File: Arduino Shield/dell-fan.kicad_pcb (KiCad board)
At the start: 2 copper layers, 101.6 x 53.3 mm, 50 parts, among them J1 Power, P1 Digital, P10 CONN_01X01, P11 CONN_01X01, P13 CONN_01X01, P2 Power, P3 Analog, P4 Analog, P5 PWM, P6 PWM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

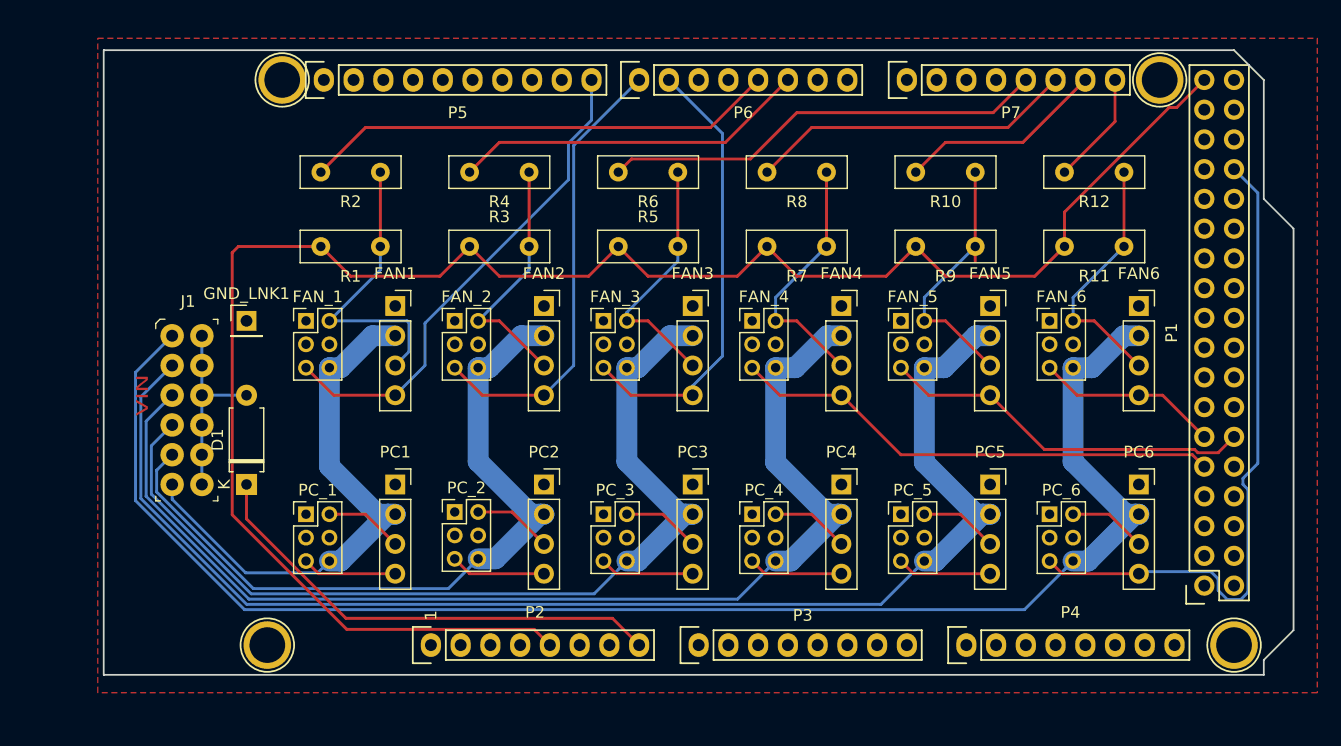
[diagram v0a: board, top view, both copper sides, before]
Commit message: moved PC Tach and PWM to D554-d69
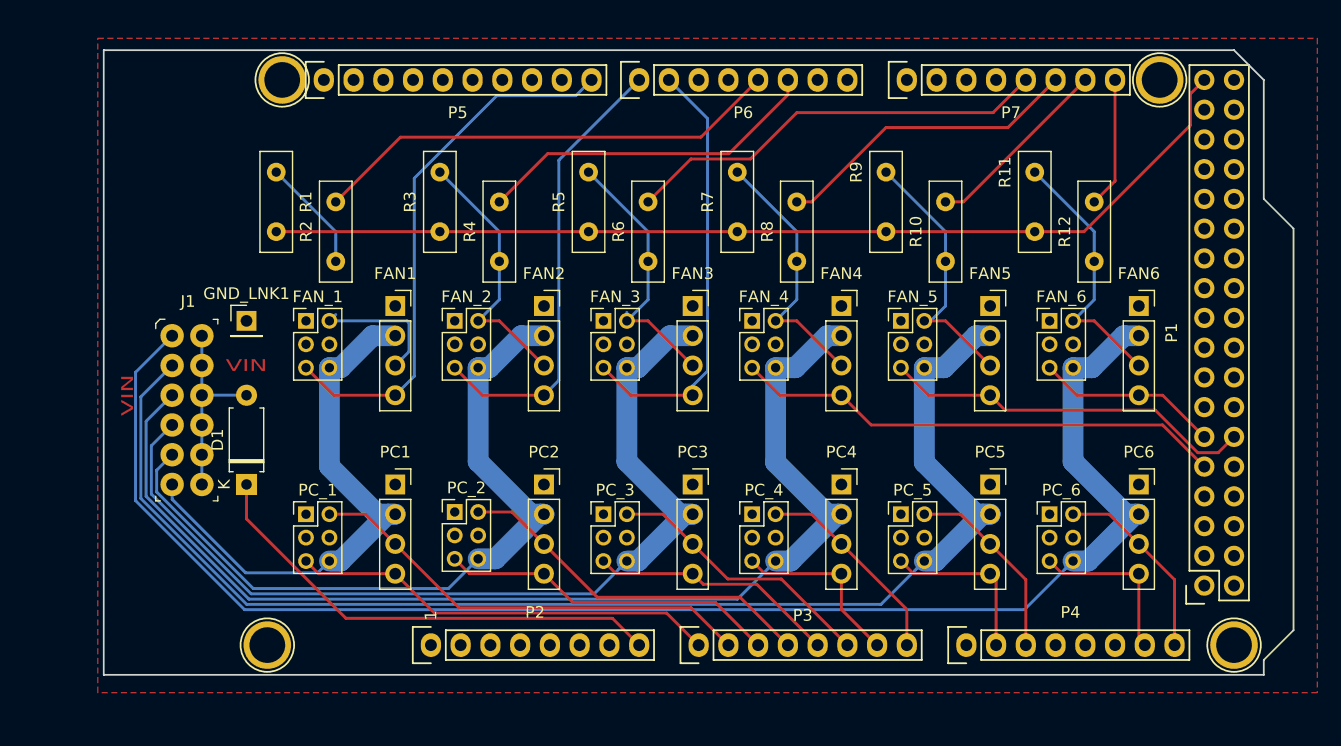
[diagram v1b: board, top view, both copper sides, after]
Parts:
- moved R1 10.9 mm to (118.1, 78.7), turned to 270 degrees
- moved R11 9.92 mm to (182.9, 78.7), turned to 270 degrees
- moved R5 9.92 mm to (144.8, 78.7), turned to 270 degrees
- moved R7 9.92 mm to (157.5, 78.7), turned to 270 degrees
- moved R9 9.92 mm to (170.2, 78.7), turned to 270 degrees
- moved R3 9.92 mm to (132.1, 78.7), turned to 270 degrees
- moved R2 8.52 mm to (123.2, 86.4), turned to 90 degrees
- moved R10 8.03 mm to (175.3, 86.4), turned to 90 degrees
- moved R12 8.03 mm to (188.0, 86.4), turned to 90 degrees
- moved R4 8.03 mm to (137.2, 86.4), turned to 90 degrees
- moved R6 8.03 mm to (149.9, 86.4), turned to 90 degrees
- moved R8 8.03 mm to (162.6, 86.4), turned to 90 degrees
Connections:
- P1 pad 19: PC5_TACH -> (no net)
- P1 pad 20: PC6_TACH -> (no net)
- P1 pad 21: PC3_TACH -> (no net)
- P1 pad 22: PC4_TACH -> (no net)
- P1 pad 23: PC1_TACH -> (no net)
- P1 pad 24: PC2_TACH -> (no net)
- P1 pad 29: PC5_PWM -> (no net)
- P1 pad 30: PC6_PWM -> (no net)
- P1 pad 31: PC3_PWM -> (no net)
- P1 pad 32: PC4_PWM -> (no net)
- P1 pad 33: PC1_PWM -> (no net)
- P1 pad 34: PC2_PWM -> (no net)
- P3 pad 1: (no net) -> PC1_PWM
- P3 pad 2: (no net) -> PC1_TACH
- P3 pad 3: (no net) -> PC2_PWM
- P3 pad 4: (no net) -> PC2_TACH
- P3 pad 5: (no net) -> PC3_PWM
- P3 pad 6: (no net) -> PC3_TACH
- P3 pad 7: (no net) -> PC4_PWM
- P3 pad 8: (no net) -> PC4_TACH
- P4 pad 2: (no net) -> PC5_PWM
- P4 pad 3: (no net) -> PC5_TACH
- P4 pad 7: (no net) -> PC6_PWM
- P4 pad 8: (no net) -> PC6_TACH
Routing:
- net +5V: track 155.5 -> 86.2 mm
- net PC6_PWM: track 56.9 -> 14.4 mm
- net PC1_TACH: track 6.67 -> 38.7 mm
- net PC1_PWM: track 8.07 -> 36.5 mm
- net PC2_TACH: track 6.75 -> 31.2 mm
- net PC2_PWM: track 8.15 -> 29.0 mm
- net PC3_TACH: track 6.67 -> 23.5 mm
- net PC3_PWM: track 8.07 -> 21.3 mm
- net PC4_TACH: track 6.67 -> 17.6 mm
- net PC6_TACH: track 6.67 -> 16.6 mm
- net PC5_TACH: track 6.67 -> 16.6 mm
- net PC4_PWM: track 8.07 -> 15.4 mm
- net PC5_PWM: track 8.07 -> 14.4 mm
- net FAN1_TACH_IN: track 25.5 -> 21.5 mm
- net FAN1_PWM: track 42.5 -> 46.4 mm
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
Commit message: fixed ground plane issue
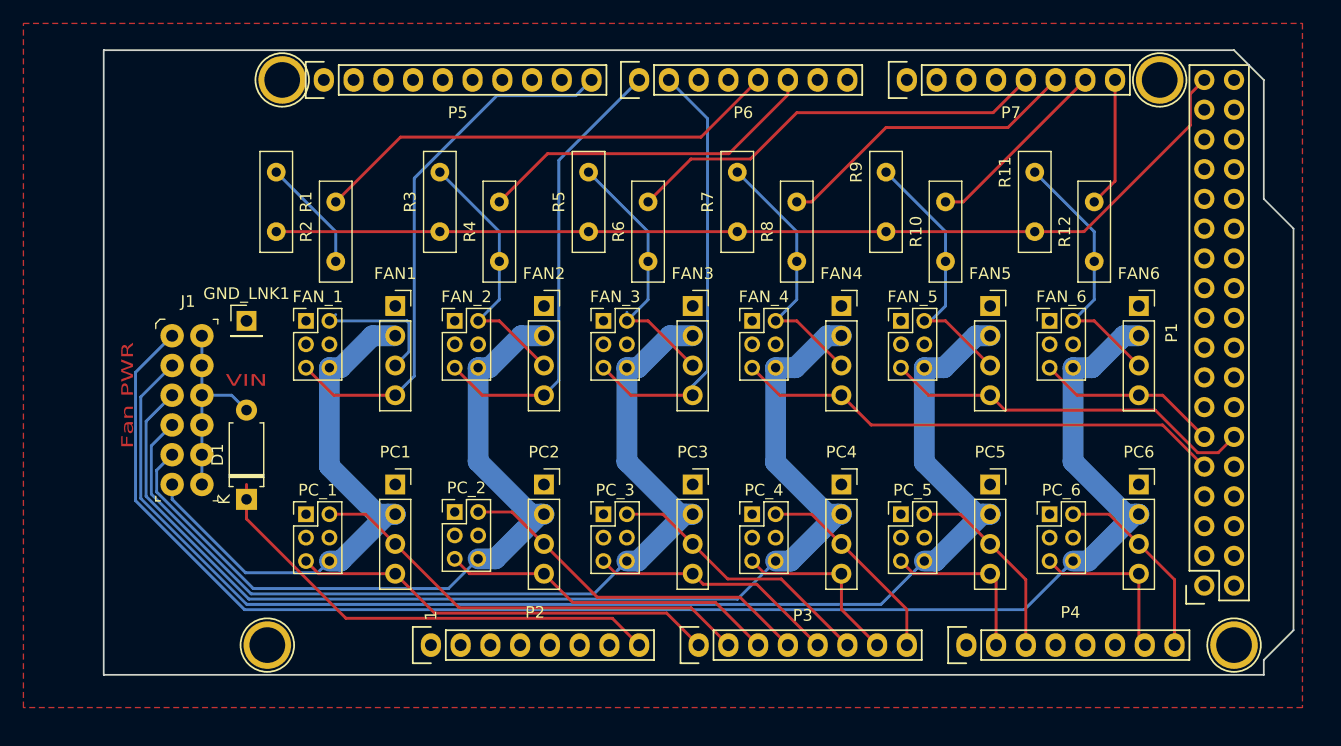
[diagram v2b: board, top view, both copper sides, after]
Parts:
- moved D1 1.27 mm to (115.6, 106.7)
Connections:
- P2 pad 5: +5V -> (no net)
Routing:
- net Net-(D1-Pad2): track 16.5 -> 17.0 mm
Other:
- board text added: "Fan PWR"
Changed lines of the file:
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@@
     (thickness 1.6)
     (drawings 20)
-    (tracks 249)
+    (tracks 250)
     (zones 0)
     (modules 50)
@@
     (add_net "Net-(P13-Pad1)")
     (add_net "Net-(P2-Pad1)")
+    (add_net "Net-(P2-Pad5)")
     (add_net "Net-(P8-Pad1)")
     (add_net "Net-(PC_1-Pad3)")
@@
   )
   (module Diode_THT:D_A-405_P7.62mm_Horizontal placed (layer F.Cu)
-    (at 115.57 105.41 90)
+    (at 115.57 106.68 90)
     (descr "Diode, A-405 series, Axial, Horizontal, pin pitch=7.62mm, , length*diameter=5.2*2.7mm^2, , http://www.diodes.com/_files/packages/A-405.pdf")
     (tags "Diode A-405 series Axial Horizontal pin pitch 7.62mm  length 5.2mm diameter 2.7mm")
@@
     (pad 3 thru_hole oval (at 5.08 0) (size 1.7272 2.032) (drill 1.016) (layers *.Cu *.Mask F.SilkS))
     (pad 4 thru_hole oval (at 7.62 0) (size 1.7272 2.032) (drill 1.016) (layers *.Cu *.Mask F.SilkS))
-    (pad 5 thru_hole oval (at 10.16 0) (size 1.7272 2.032) (drill 1.016) (layers *.Cu *.Mask F.SilkS)
-      (net 2 +5V))
+    (pad 5 thru_hole oval (at 10.16 0) (size 1.7272 2.032) (drill 1.016) (layers *.Cu *.Mask F.SilkS))
     (pad 6 thru_hole oval (at 12.7 0) (size 1.7272 2.032) (drill 1.016) (layers *.Cu *.Mask F.SilkS)
       (net 1 GND))
@@
     (pad 1 thru_hole circle (at 0 0) (size 4.064 4.064) (drill 3.048) (layers *.Cu *.Mask F.SilkS))
   )
-  (gr_text VIN (at 115.57 95.25) (layer F.Cu)
+  (gr_text VIN (at 115.57 96.52) (layer F.Cu)
     (effects (font (size 1 1.5) (thickness 0.25)))
   )
-  (gr_text VIN (at 105.41 97.79 90) (layer F.Cu)
+  (gr_text "Fan PWR" (at 105.41 97.79 90) (layer F.Cu)
     (effects (font (size 1 1.5) (thickness 0.25)))
   )
@@
   (segment (start 154.37401 75.74999) (end 128.72001 75.74999) (width 0.25) (layer F.Cu) (net 6))
   (segment (start 159.258 70.866) (end 154.37401 75.74999) (width 0.25) (layer F.Cu) (net 6))
-  (segment (start 111.76 97.79) (end 115.57 97.79) (width 0.25) (layer B.Cu) (net 7))
   (segment (start 111.76 105.41) (end 111.76 92.71) (width 0.25) (layer B.Cu) (net 7))
   (segment (start 140.638798 107.95) (end 140.97 107.95) (width 1.78) (layer B.Cu) (net 8))
@@
   (segment (start 140.97 113.03) (end 143.429972 115.489972) (width 0.25) (layer F.Cu) (net 27))
   (segment (start 199.898 73.406) (end 200.406 73.406) (width 0.25) (layer F.Cu) (net 0))
+  (segment (start 114.3 97.79) (end 115.57 99.06) (width 0.25) (layer B.Cu) (net 7))
+  (segment (start 111.76 97.79) (end 114.3 97.79) (width 0.25) (layer B.Cu) (net 7))
   (segment (start 168.91 100.33) (end 166.37 97.79) (width 0.25) (layer F.Cu) (net 13))
   (segment (start 193.802 100.33) (end 168.91 100.33) (width 0.25) (layer F.Cu) (net 13))
@@
     (polygon
       (pts
-        (xy 207.01 123.19) (xy 102.87 123.19) (xy 102.87 67.31) (xy 207.01 67.31)
+        (xy 205.74 124.46) (xy 96.52 124.46) (xy 96.52 66.04) (xy 205.74 66.04)
       )
     )

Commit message: No interrupts means better pin placement
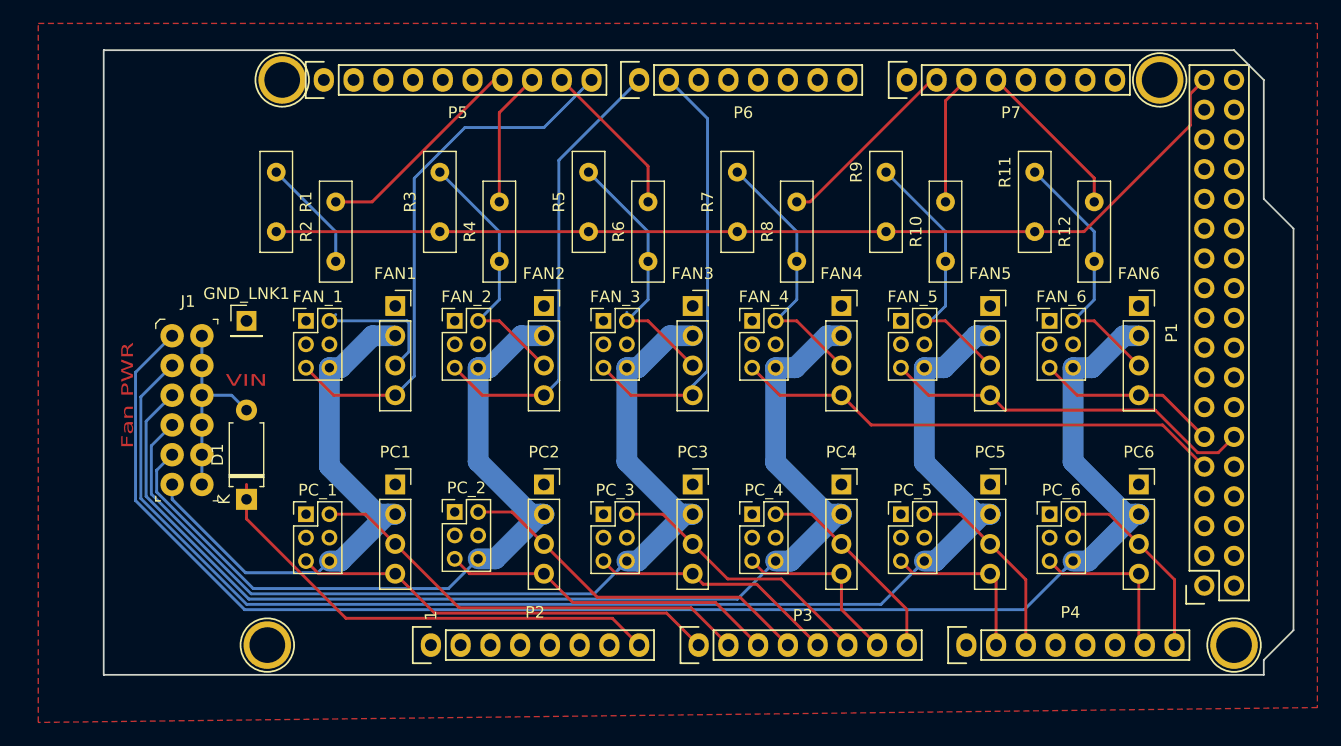
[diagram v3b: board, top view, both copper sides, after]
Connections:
- P5 pad 7: (no net) -> FAN1_TACH
- P5 pad 8: (no net) -> FAN2_TACH
- P5 pad 9: (no net) -> FAN3_TACH
- P6 pad 5: FAN1_TACH -> (no net)
- P6 pad 6: FAN2_TACH -> (no net)
- P7 pad 2: (no net) -> FAN4_TACH
- P7 pad 3: (no net) -> FAN5_TACH
- P7 pad 4: (no net) -> FAN6_TACH
- P7 pad 5: FAN3_TACH -> (no net)
- P7 pad 6: FAN4_TACH -> (no net)
- P7 pad 7: FAN5_TACH -> (no net)
- P7 pad 8: FAN6_TACH -> (no net)
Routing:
- net FAN3_TACH: track 36.6 -> 13.5 mm
- net FAN1_TACH: track 40.4 -> 18.5 mm
- net FAN2_TACH: track 29.7 -> 11.6 mm
- net FAN4_TACH: track 26.4 -> 16.3 mm
- net FAN5_TACH: track 16.4 -> 11.2 mm
- net FAN6_TACH: track 11.2 -> 13.9 mm

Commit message: commiting prototype run with gerber files
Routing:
- net (no net): track 0.65 -> 0.00 mm
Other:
- board text added: "Fan Interceptor"
- board text added: "Rev 1.00"
- board text added: "© 2021"

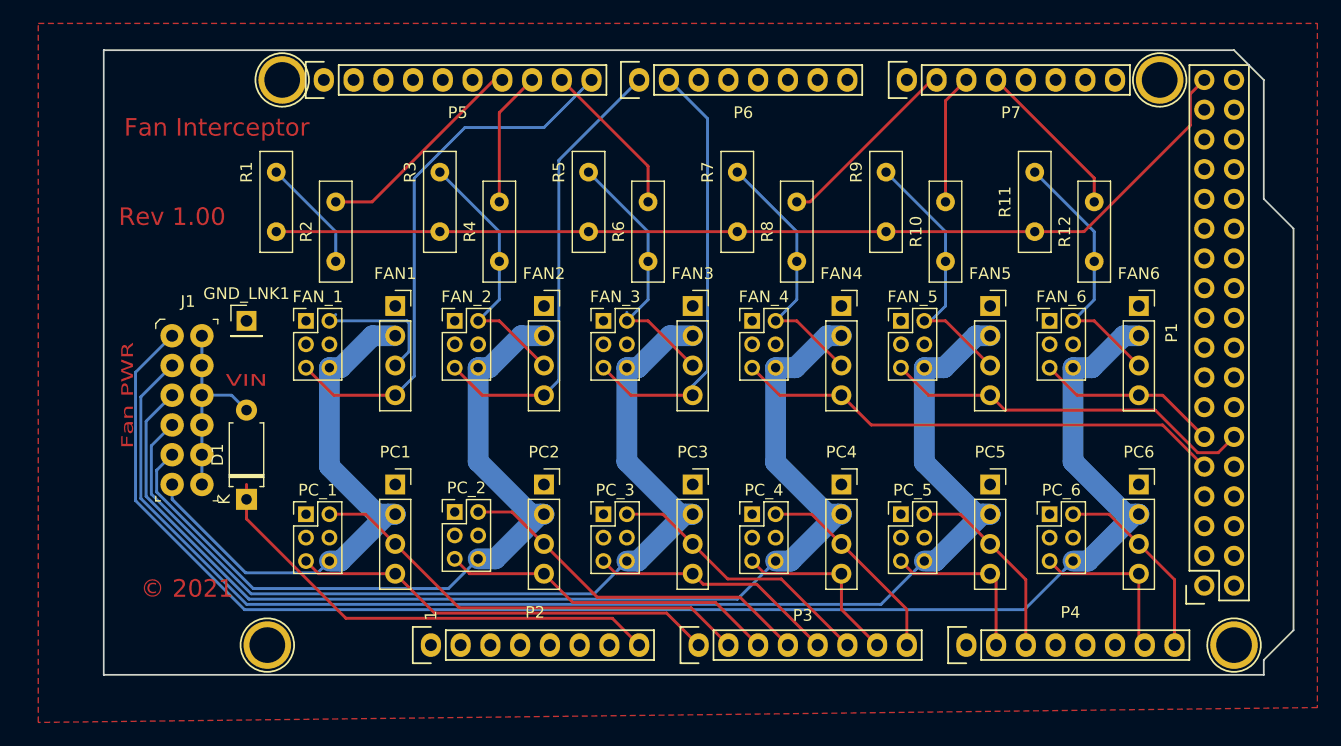
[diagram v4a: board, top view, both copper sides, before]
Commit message: fixing two missing traces from production prototype
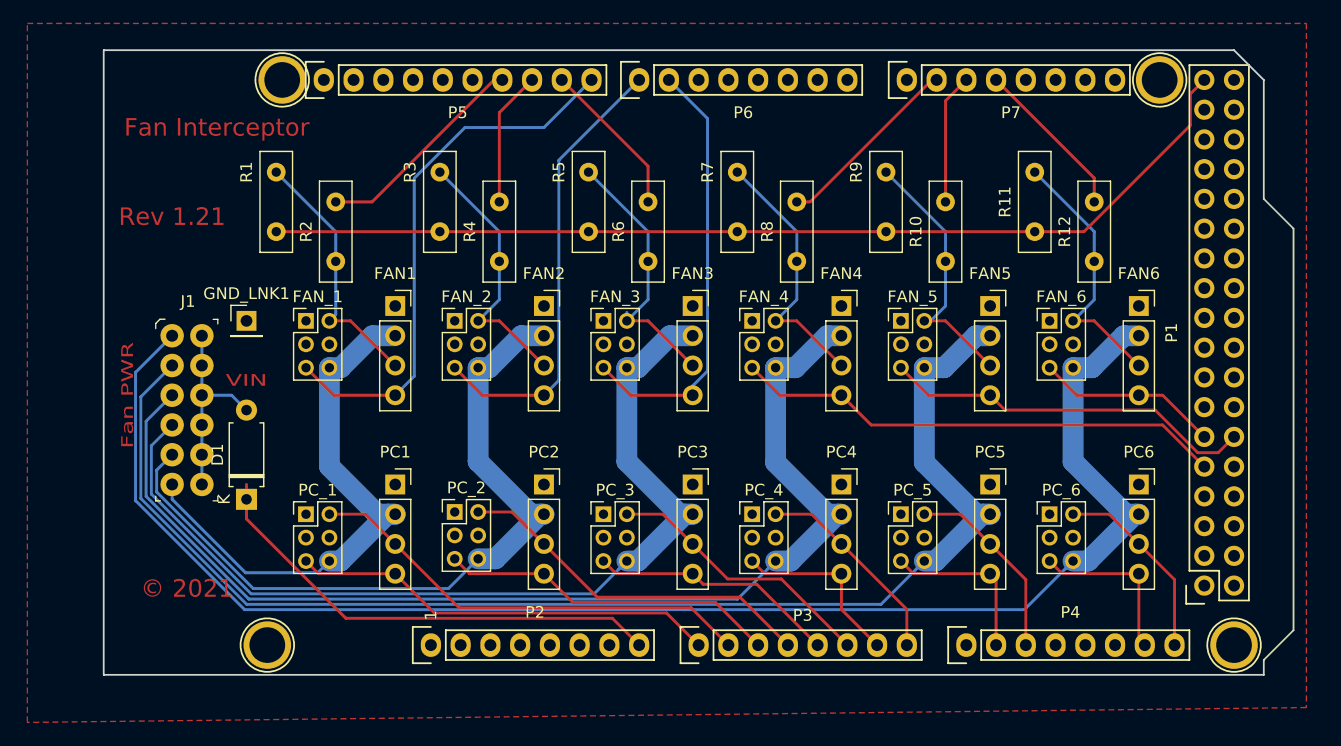
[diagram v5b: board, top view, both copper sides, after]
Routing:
- net FAN1_TACH_IN: track 21.5 -> 22.2 mm
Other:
- board text added: "Rev 1.21"
- board text removed: "Rev 1.00"
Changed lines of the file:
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@@
     (thickness 1.6)
     (drawings 23)
-    (tracks 242)
+    (tracks 241)
     (zones 0)
     (modules 50)
@@
     (effects (font (size 1.5 1.5) (thickness 0.3)))
   )
-  (gr_text "Rev 1.00" (at 109.22 82.55) (layer F.Cu)
+  (gr_text "Rev 1.21" (at 109.22 82.55) (layer F.Cu)
     (effects (font (size 1.5 1.5) (thickness 0.3)))
   )
@@
   (segment (start 175.26 72.644) (end 177.038 70.866) (width 0.25) (layer F.Cu) (net 34))
   (segment (start 175.26 81.28) (end 175.26 72.644) (width 0.25) (layer F.Cu) (net 34))
-  (segment (start 129.445001 94.074999) (end 128.27 95.25) (width 0.25) (layer B.Cu) (net 35))
-  (segment (start 129.445001 91.599999) (end 129.445001 94.074999) (width 0.25) (layer B.Cu) (net 35))
-  (segment (start 129.285002 91.44) (end 129.445001 91.599999) (width 0.25) (layer B.Cu) (net 35))
-  (segment (start 122.65 91.44) (end 129.285002 91.44) (width 0.25) (layer B.Cu) (net 35))
-  (segment (start 123.19 90.9) (end 122.65 91.44) (width 0.25) (layer B.Cu) (net 35))
   (segment (start 123.19 83.82) (end 118.11 78.74) (width 0.25) (layer B.Cu) (net 35))
   (segment (start 123.19 86.36) (end 123.19 83.82) (width 0.25) (layer B.Cu) (net 35))
+  (segment (start 124.46 91.44) (end 128.27 95.25) (width 0.25) (layer F.Cu) (net 35))
+  (segment (start 122.65 91.44) (end 124.46 91.44) (width 0.25) (layer F.Cu) (net 35))
+  (segment (start 123.19 90.9) (end 122.65 91.44) (width 0.25) (layer B.Cu) (net 35))
+  (segment (start 123.19 86.36) (end 123.19 90.9) (width 0.25) (layer B.Cu) (net 35))
   (segment (start 137.16 91.44) (end 140.97 95.25) (width 0.25) (layer F.Cu) (net 36))
   (segment (start 135.35 91.44) (end 137.16 91.44) (width 0.25) (layer F.Cu) (net 36))
@@
     (polygon
       (pts
-        (xy 207.01 124.46) (xy 97.79 125.73) (xy 97.79 66.04) (xy 207.01 66.04)
+        (xy 206.073072 124.46) (xy 96.853072 125.73) (xy 96.853072 66.04) (xy 206.073072 66.04)
       )
     )
